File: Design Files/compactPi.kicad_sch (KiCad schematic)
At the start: 8 parts, among them J15 USB_C_Receptacle_USB2.0, U22 WE-TVS-82400102, U23 WE-TVS-82400102

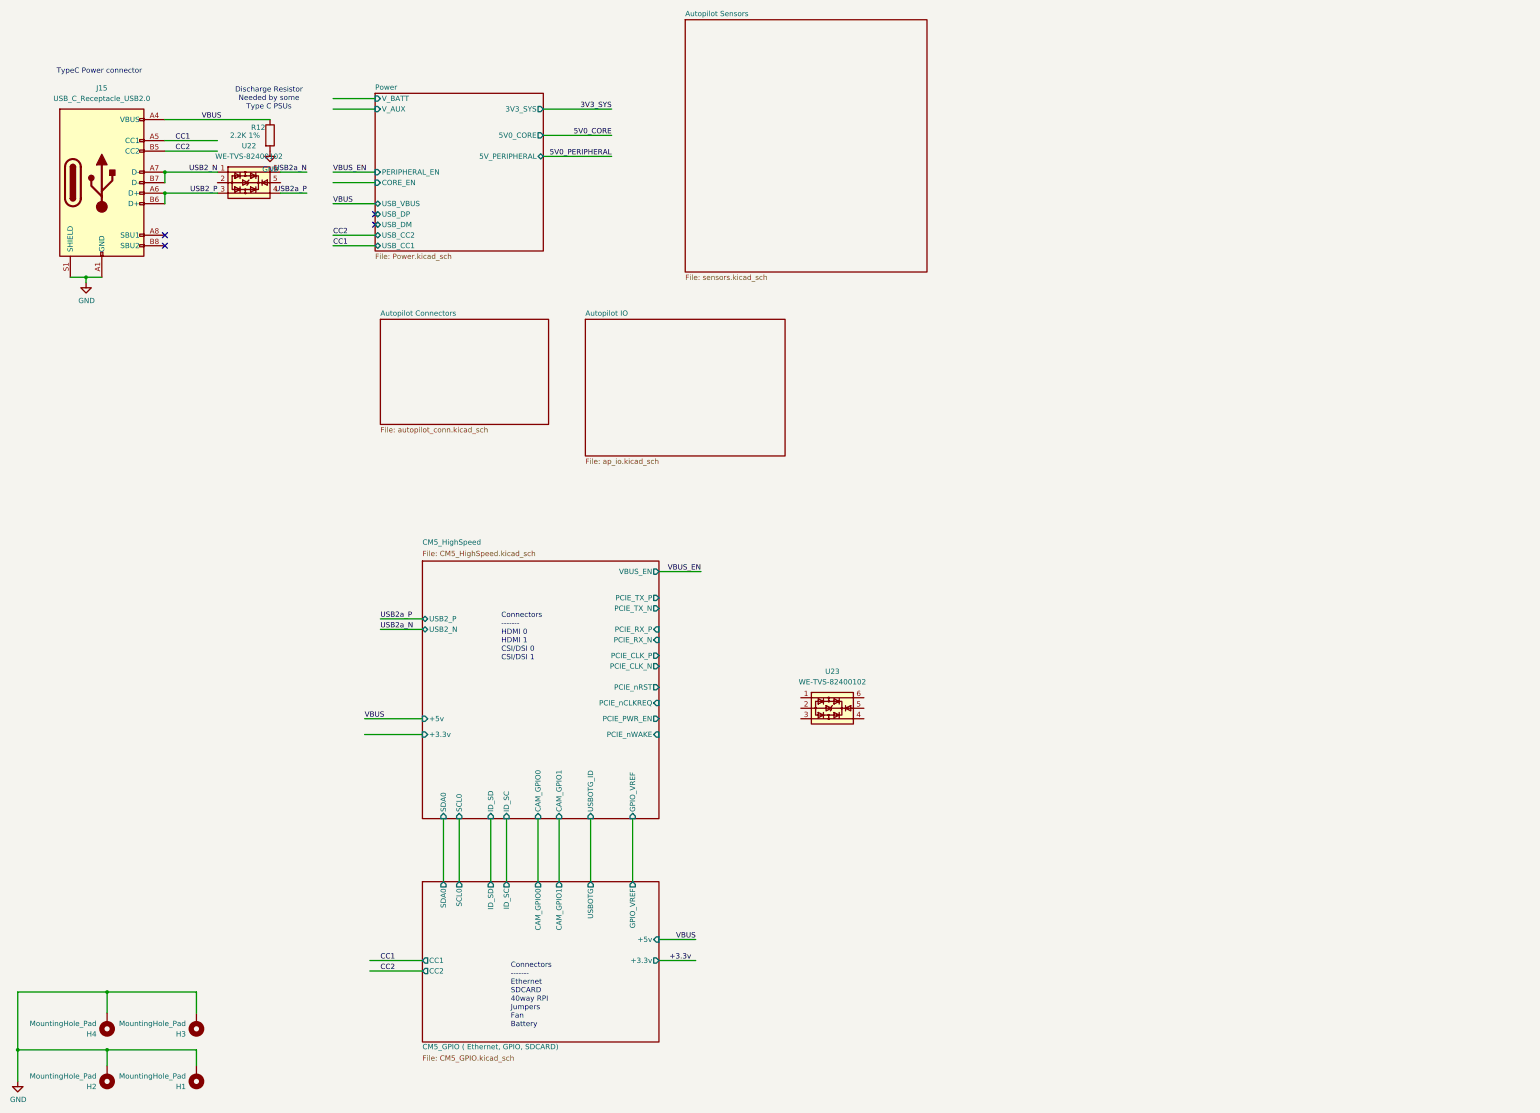
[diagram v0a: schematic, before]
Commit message: Prelim work on autopilot sensors complete
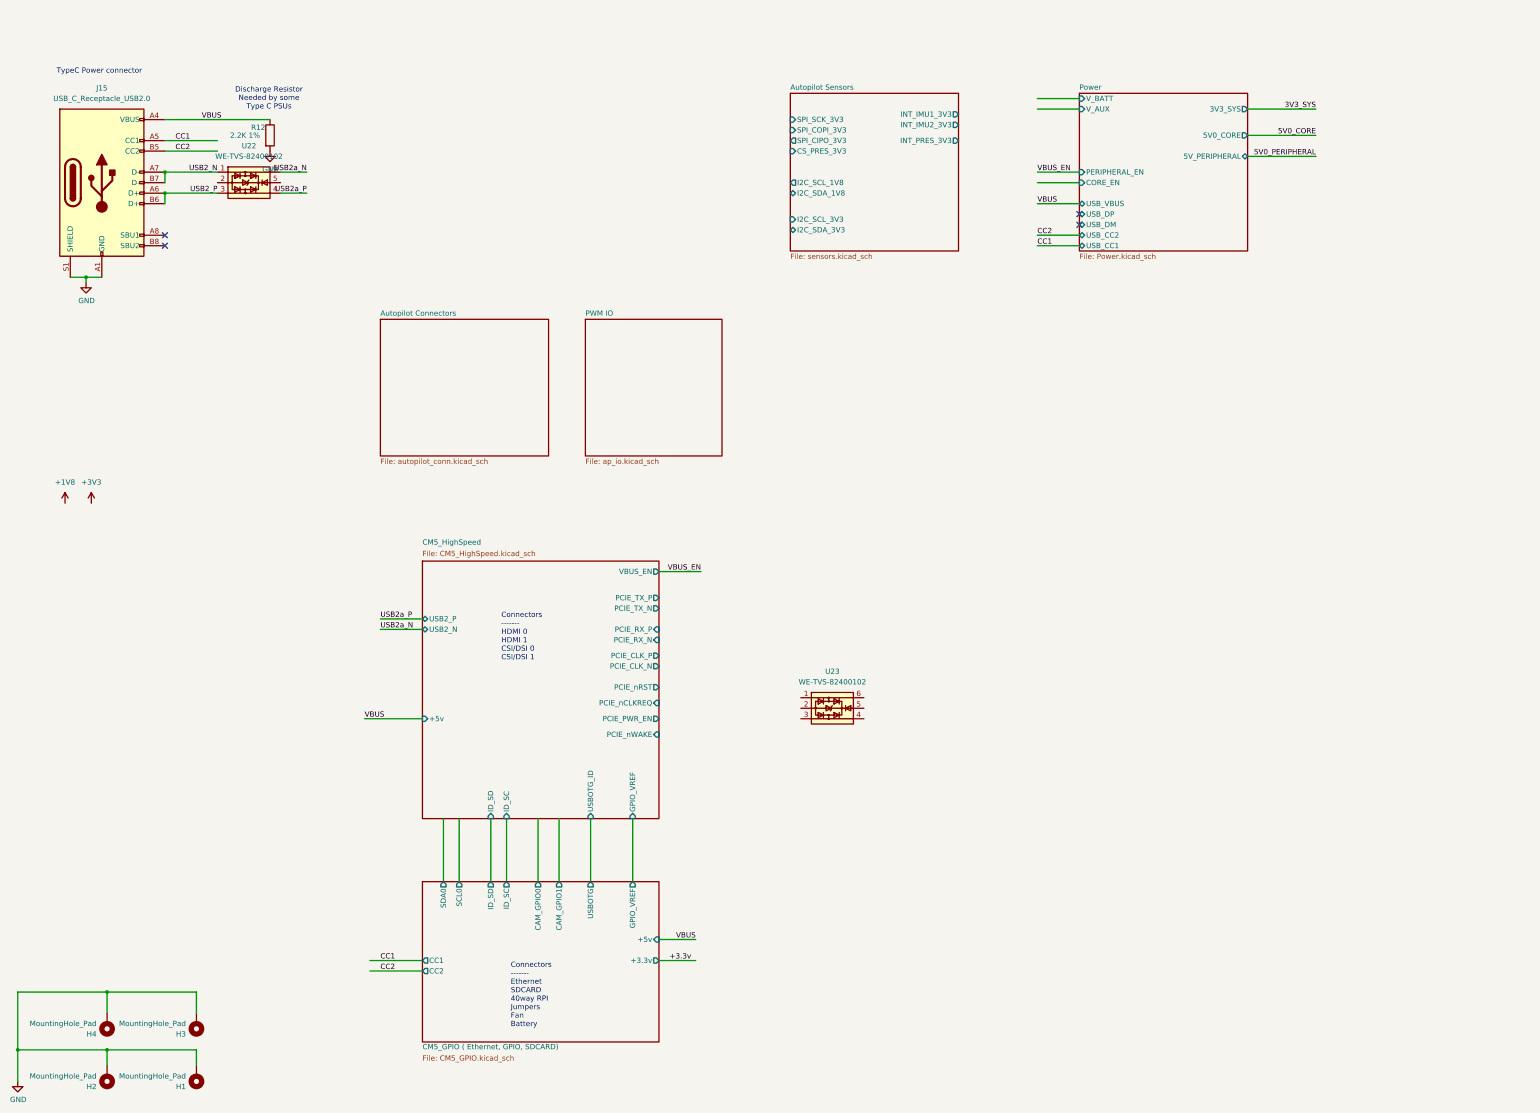
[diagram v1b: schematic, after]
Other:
- sheet Autopilot IO renamed PWM IO
- sheet Autopilot Sensors ports: added CS_PRES_3V3, I2C_SCL_1V8, I2C_SCL_3V3, I2C_SDA_1V8, I2C_SDA_3V3, INT_IMU1_3V3, INT_IMU2_3V3, INT_PRES_3V3, SPI_CIPO_3V3, SPI_COPI_3V3, SPI_SCK_3V3; removed none
- sheet CM5_HighSpeed ports: added none; removed +3.3v, CAM_GPIO0, CAM_GPIO1, SCL0, SDA0

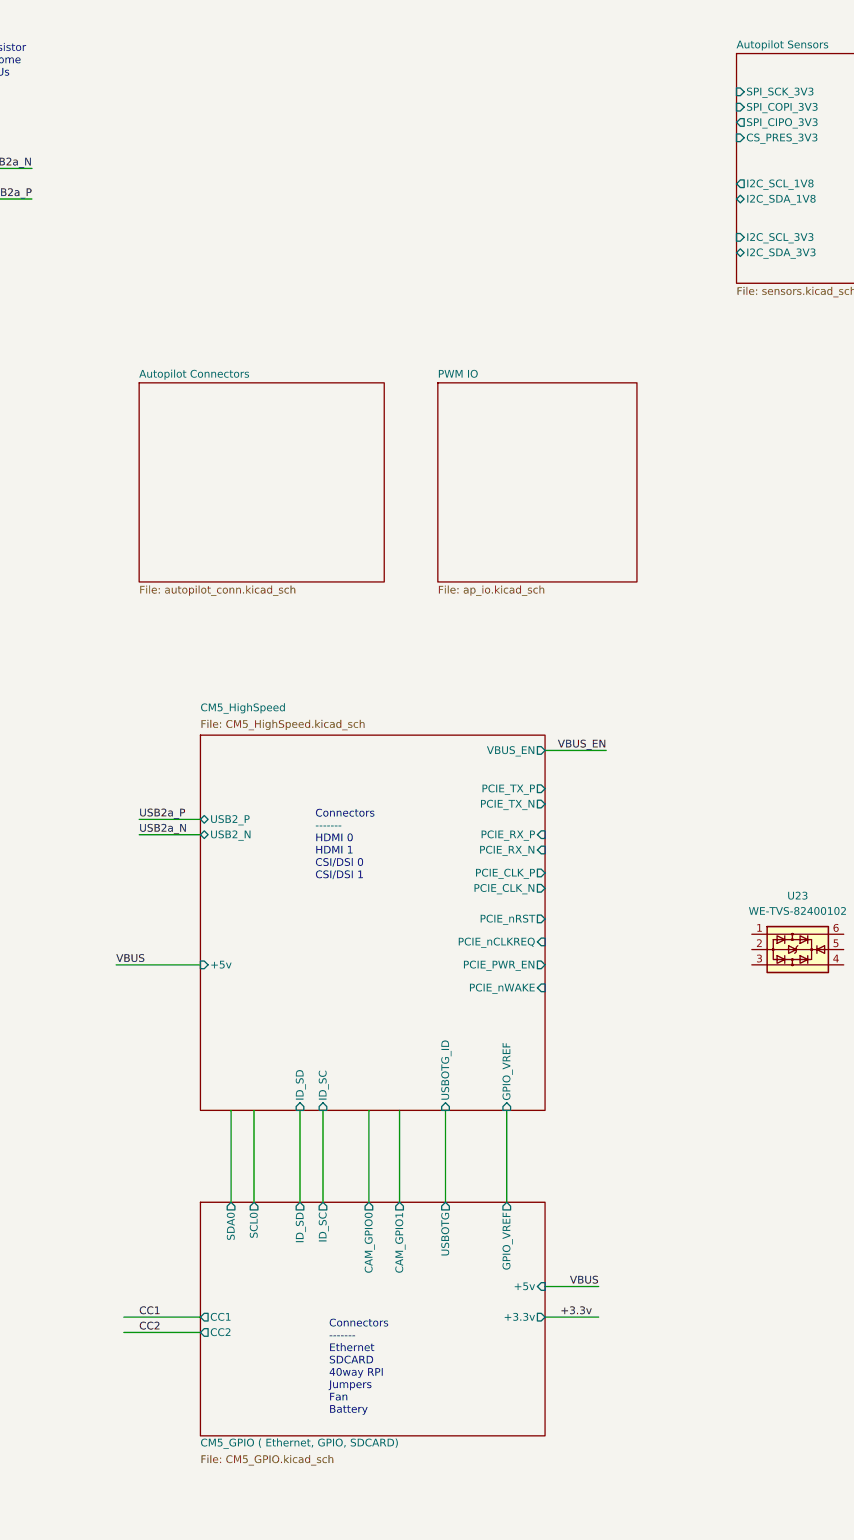
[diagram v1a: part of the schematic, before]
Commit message: Continued adding GPIO interfaces
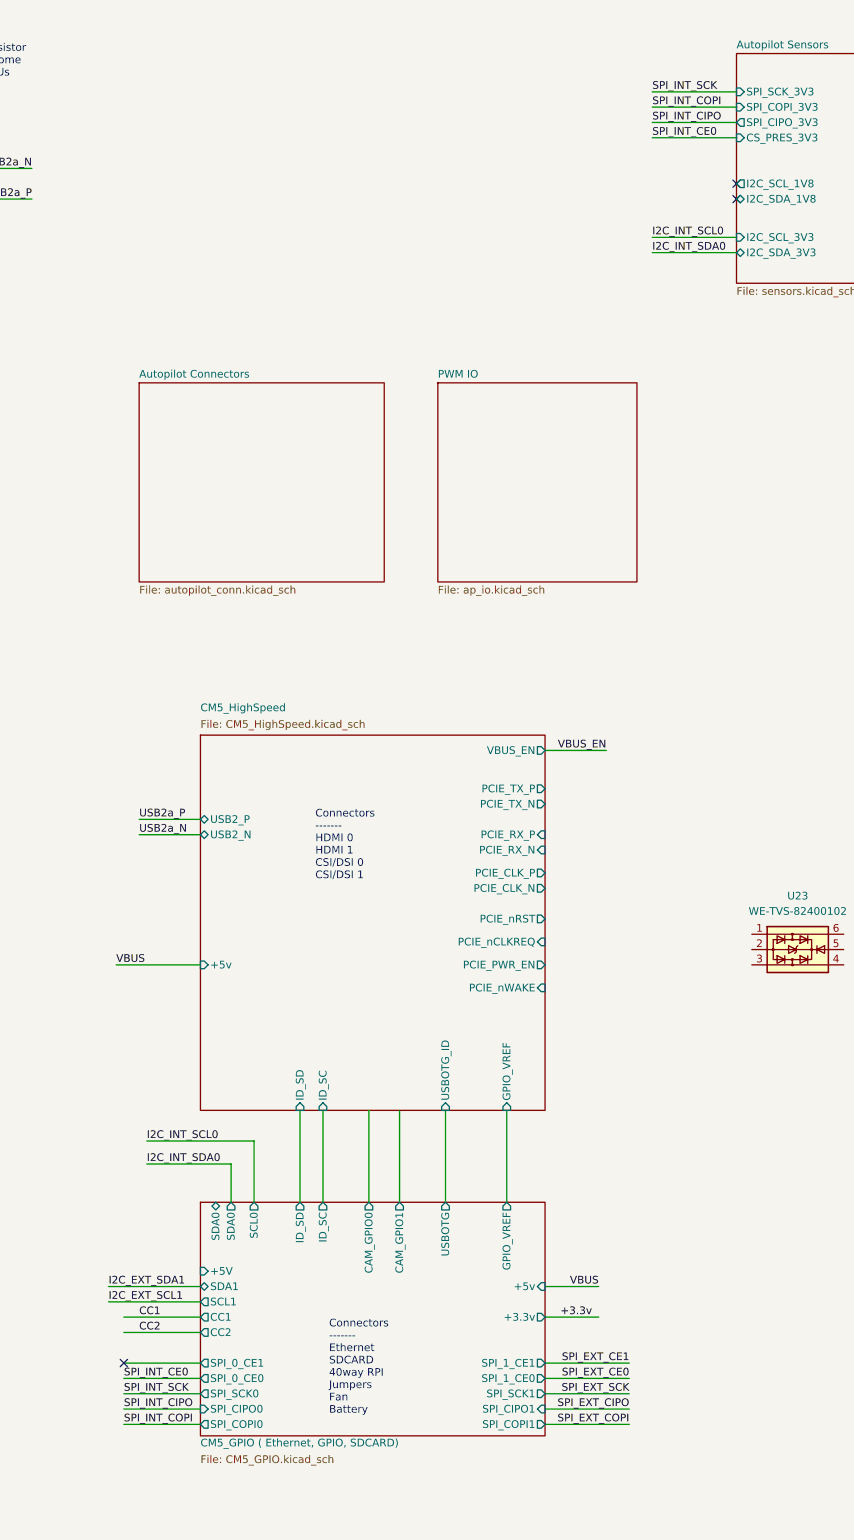
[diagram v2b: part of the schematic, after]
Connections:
- no-connect marks 4 -> 7
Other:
- sheet CM5_GPIO ( Ethernet, GPIO, SDCARD) ports: added +5V, SCL1, SDA1, SPI_0_CE0, SPI_0_CE1, SPI_1_CE0, SPI_1_CE1, SPI_CIPO0, SPI_CIPO1, SPI_COPI0, SPI_COPI1, SPI_SCK0, SPI_SCK1; removed none

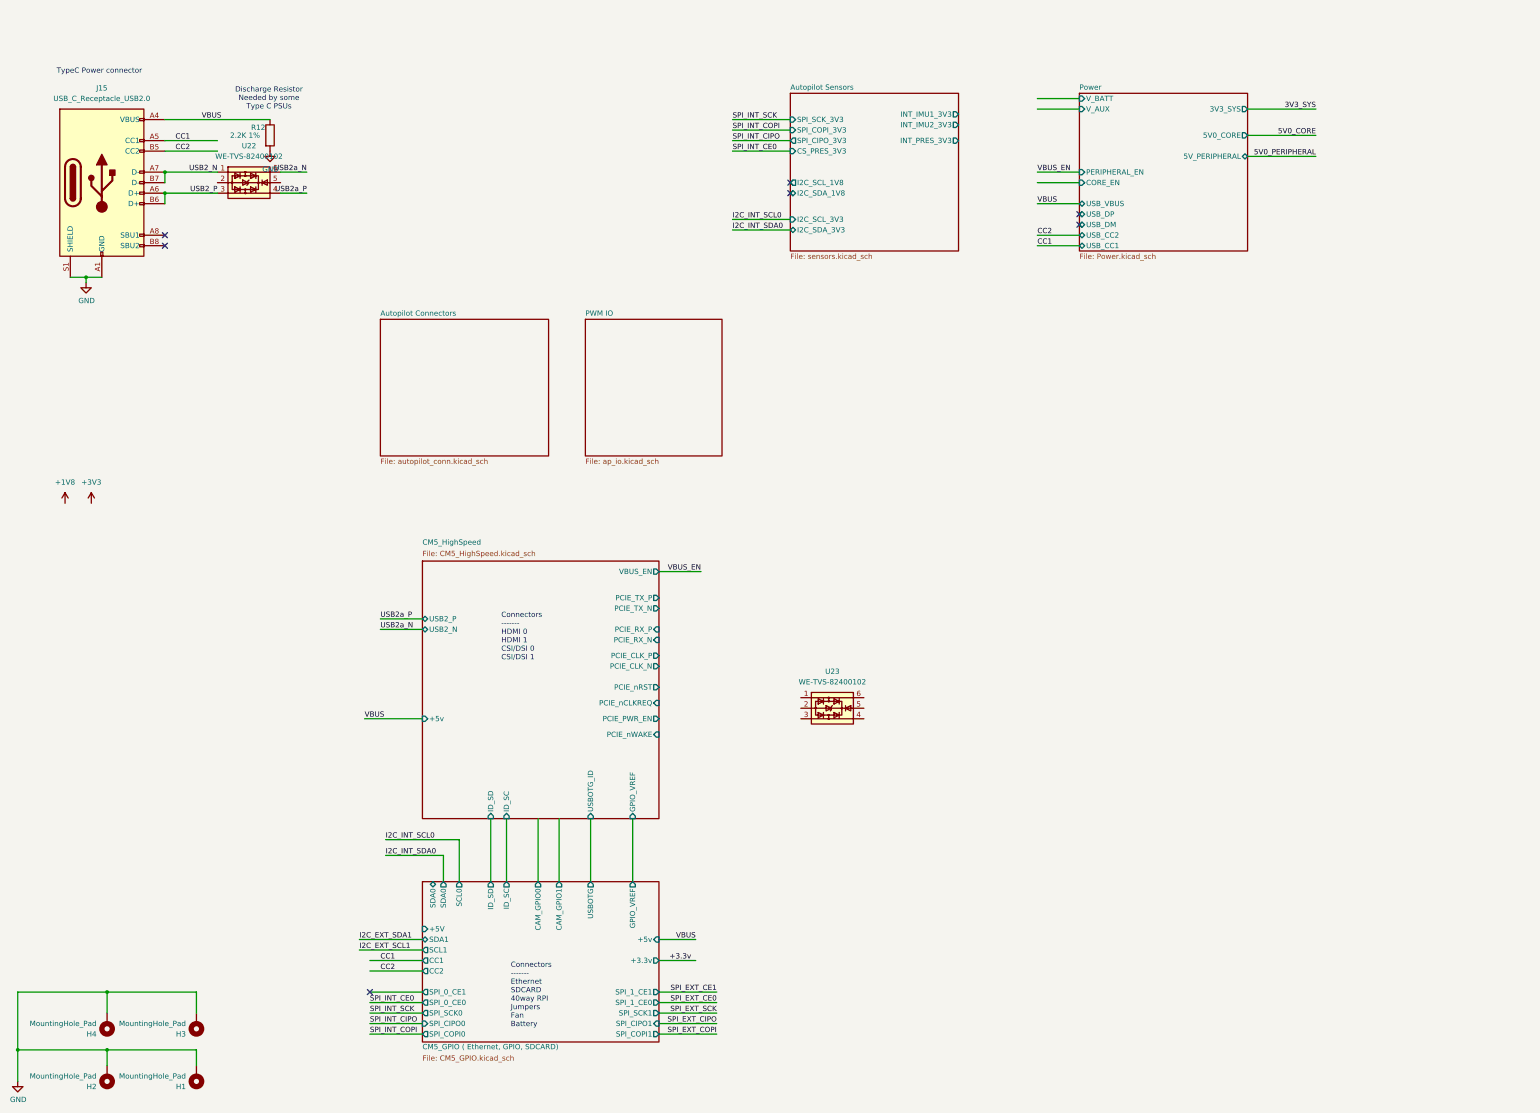
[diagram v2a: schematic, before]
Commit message: More interface interconnects
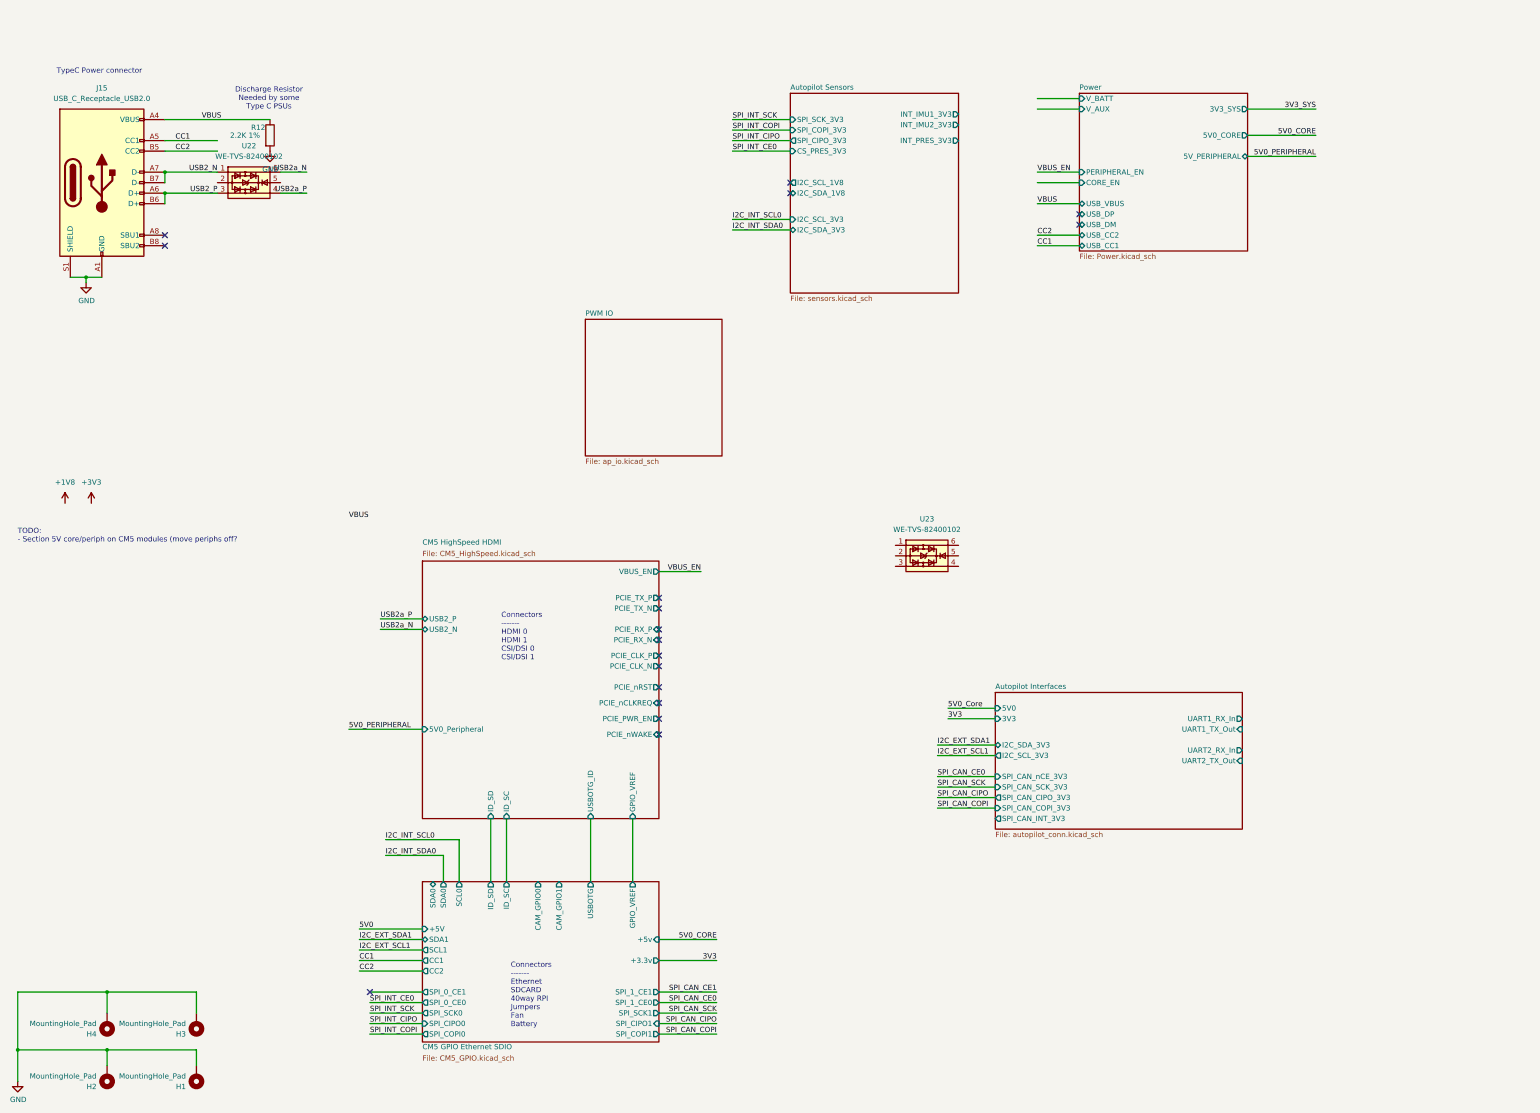
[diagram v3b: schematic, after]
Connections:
- no-connect marks 7 -> 17
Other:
- sheet Autopilot Connectors renamed Autopilot Interfaces
- sheet CM5_GPIO ( Ethernet, GPIO, SDCARD) renamed CM5 GPIO Ethernet SDIO
- sheet CM5_HighSpeed renamed CM5 HighSpeed HDMI
- sheet Autopilot Interfaces ports: added 3V3, 5V0, I2C_SCL_3V3, I2C_SDA_3V3, SPI_CAN_CIPO_3V3, SPI_CAN_COPI_3V3, SPI_CAN_INT_3V3, SPI_CAN_SCK_3V3, SPI_CAN_nCE_3V3, UART1_RX_In, UART1_TX_Out, UART2_RX_In, UART2_TX_Out; removed none
- sheet CM5 HighSpeed HDMI ports: added 5V0_Peripheral; removed +5v
- note added: "TODO: - Section 5V core/periph on CM5 modules (move periphs off?"
- moved on the sheet: U23
